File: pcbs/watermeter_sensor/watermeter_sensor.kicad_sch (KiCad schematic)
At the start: 14 parts, among them J1 Conn_01x06, U1 LDC2112, U2 MCP1811A

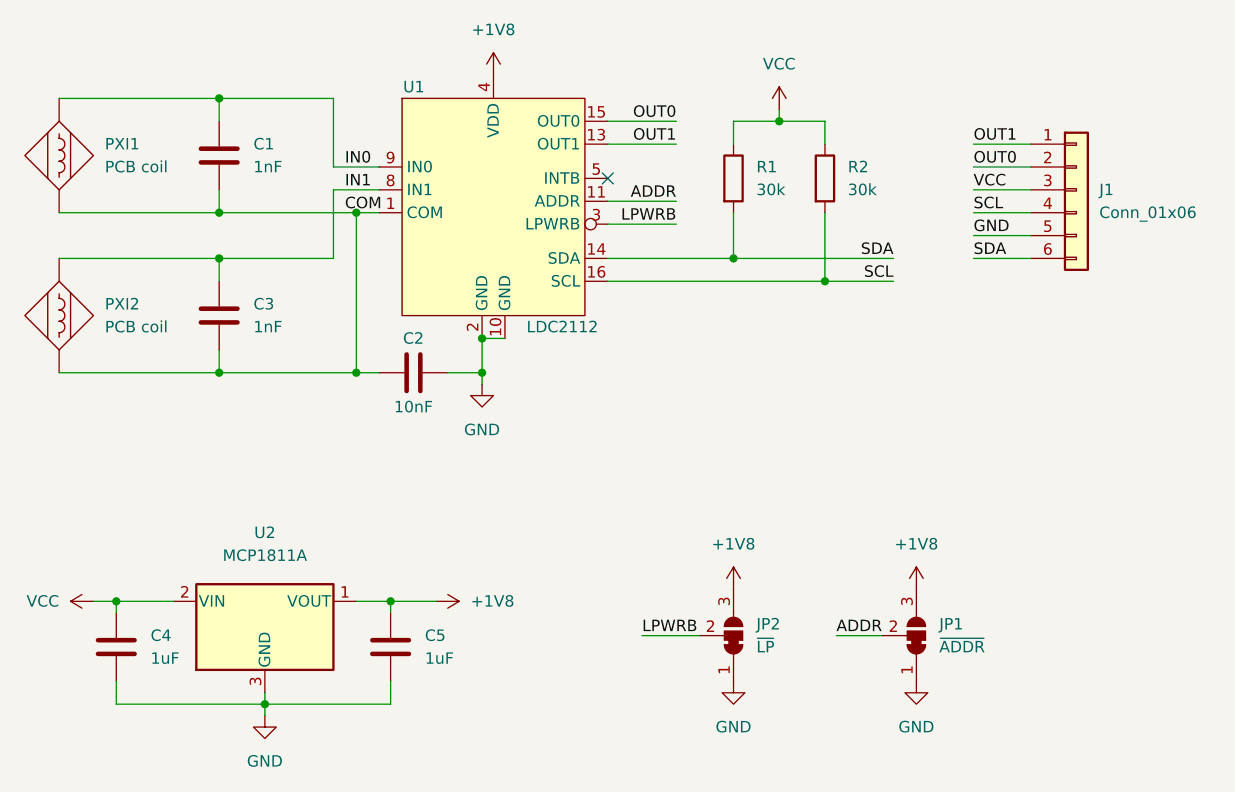
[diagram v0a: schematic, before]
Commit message: chore: Update .gitignore, upgrade to KiCAD 8
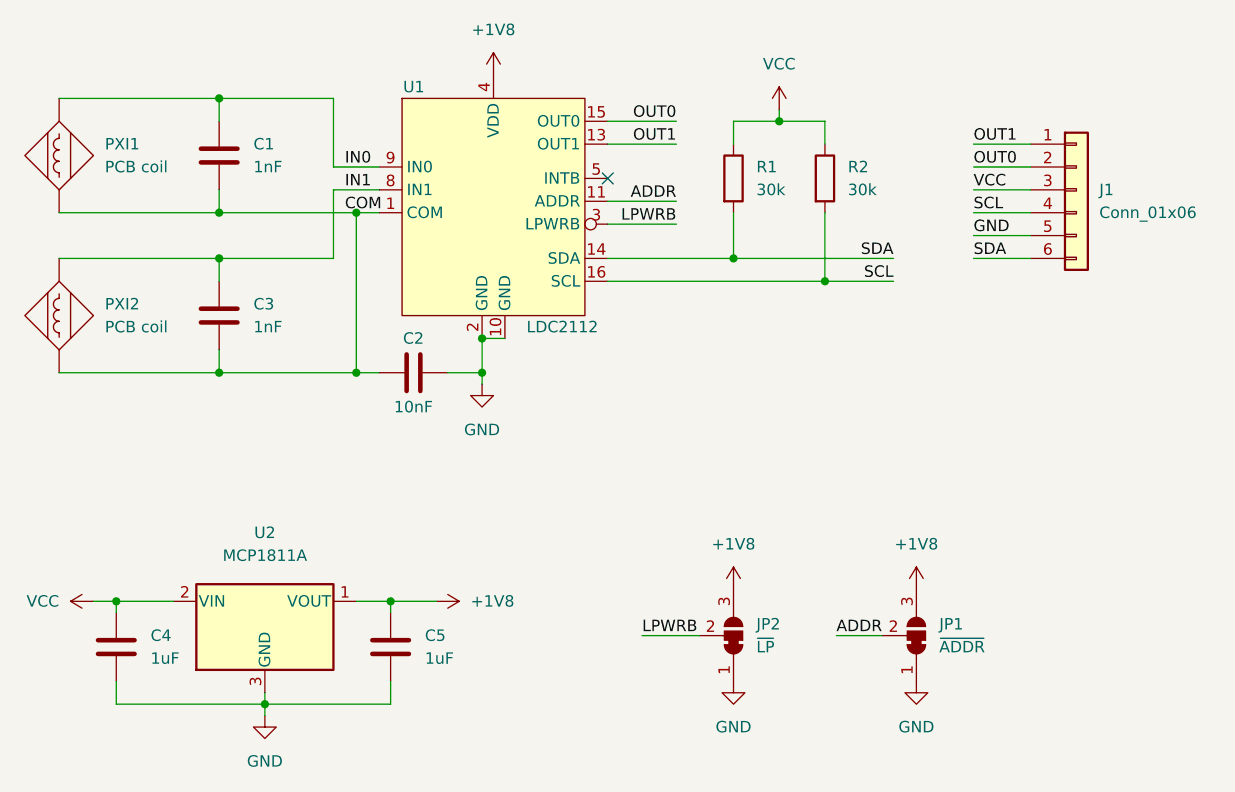
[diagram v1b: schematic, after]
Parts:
- PXI1, PXI2: Spice_Model 1uH -> (none); Spice_Netlist_Enabled Y -> (none); Spice_Primitive L -> (none)
